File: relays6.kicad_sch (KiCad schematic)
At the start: 1 part

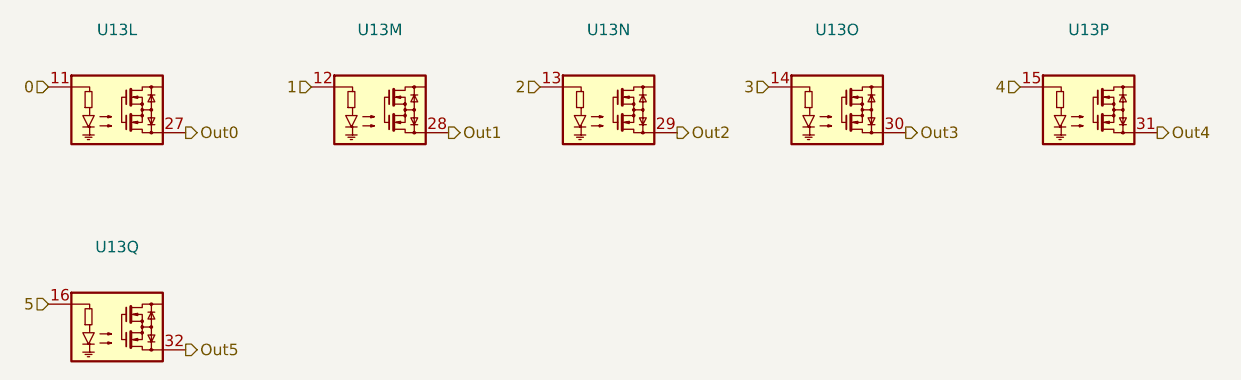
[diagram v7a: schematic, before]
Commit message: added footprints for modules
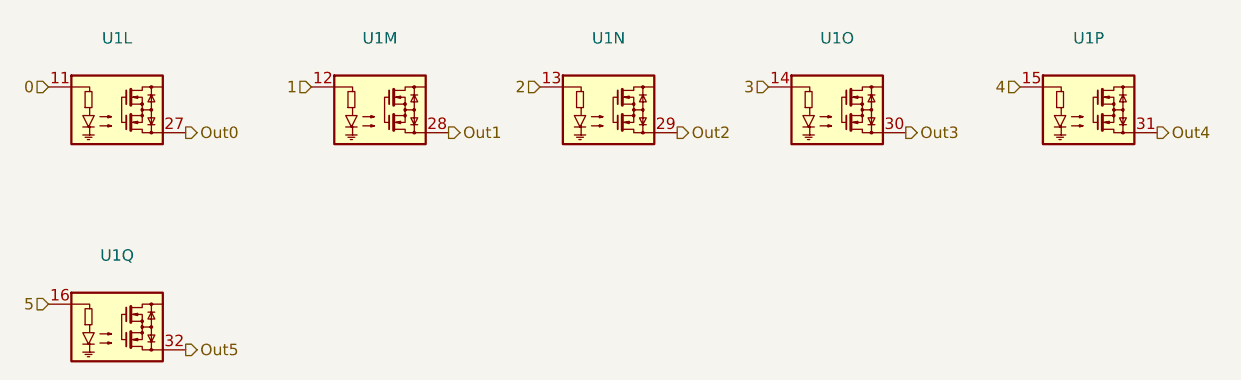
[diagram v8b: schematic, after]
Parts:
- U1: renamed from U13; footprint (none) -> custom:module_ssr
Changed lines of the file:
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@@
 		(dnp no)
 		(fields_autoplaced yes)
-		(property "Reference" "U13"
-			(at 180.34 83.82 0)
+		(property "Reference" "U1"
+			(at 180.34 84.7555 0)
 			(effects
 				(font
@@
 		)
 		(property "Value" "~"
-			(at 180.34 86.36 0)
-			(effects
-				(font
-					(size 1.27 1.27)
-				)
-			)
-		)
-		(property "Footprint" ""
+			(at 180.34 87.1798 0)
+			(effects
+				(font
+					(size 1.27 1.27)
+				)
+			)
+		)
+		(property "Footprint" "custom:module_ssr"
 			(at 176.53 87.63 0)
 			(effects
@@
 			(project "transistor-clock"
 				(path "/ce10d5bc-995e-4952-aa76-0a08f713a0f2/2c36a9e9-de42-4705-9ad4-94f4cc168e2f/a7714f05-6baa-4e42-8e1d-8ccd75369c94"
-					(reference "U13")
+					(reference "U1")
 					(unit 16)
 				)
 				(path "/ce10d5bc-995e-4952-aa76-0a08f713a0f2/2c36a9e9-de42-4705-9ad4-94f4cc168e2f/c8a6393e-4b34-48bb-b57a-38ecbb8960e5"
-					(reference "U23")
-					(unit 2)
+					(reference "U2")
+					(unit 16)
 				)
 			)
@@
 		(dnp no)
 		(fields_autoplaced yes)
-		(property "Reference" "U13"
-			(at 127 83.82 0)
+		(property "Reference" "U1"
+			(at 127 84.7555 0)
 			(effects
 				(font
@@
 		)
 		(property "Value" "~"
-			(at 127 86.36 0)
-			(effects
-				(font
-					(size 1.27 1.27)
-				)
-			)
-		)
-		(property "Footprint" ""
+			(at 127 87.1798 0)
+			(effects
+				(font
+					(size 1.27 1.27)
+				)
+			)
+		)
+		(property "Footprint" "custom:module_ssr"
 			(at 123.19 87.63 0)
 			(effects
@@
 			(project "transistor-clock"
 				(path "/ce10d5bc-995e-4952-aa76-0a08f713a0f2/2c36a9e9-de42-4705-9ad4-94f4cc168e2f/a7714f05-6baa-4e42-8e1d-8ccd75369c94"
-					(reference "U13")
+					(reference "U1")
 					(unit 14)
 				)
 				(path "/ce10d5bc-995e-4952-aa76-0a08f713a0f2/2c36a9e9-de42-4705-9ad4-94f4cc168e2f/c8a6393e-4b34-48bb-b57a-38ecbb8960e5"
-					(reference "U19")
-					(unit 2)
+					(reference "U2")
+					(unit 14)
 				)
 			)
@@
 		(dnp no)
 		(fields_autoplaced yes)
-		(property "Reference" "U13"
-			(at 72.39 107.95 0)
+		(property "Reference" "U1"
+			(at 72.39 108.8855 0)
 			(effects
 				(font
@@
 		)
 		(property "Value" "~"
-			(at 72.39 110.49 0)
-			(effects
-				(font
-					(size 1.27 1.27)
-				)
-			)
-		)
-		(property "Footprint" ""
+			(at 72.39 111.3098 0)
+			(effects
+				(font
+					(size 1.27 1.27)
+				)
+			)
+		)
+		(property "Footprint" "custom:module_ssr"
 			(at 68.58 111.76 0)
 			(effects
@@
 			(project "transistor-clock"
 				(path "/ce10d5bc-995e-4952-aa76-0a08f713a0f2/2c36a9e9-de42-4705-9ad4-94f4cc168e2f/a7714f05-6baa-4e42-8e1d-8ccd75369c94"
-					(reference "U13")
+					(reference "U1")
 					(unit 17)
 				)
 				(path "/ce10d5bc-995e-4952-aa76-0a08f713a0f2/2c36a9e9-de42-4705-9ad4-94f4cc168e2f/c8a6393e-4b34-48bb-b57a-38ecbb8960e5"
-					(reference "U25")
-					(unit 2)
+					(reference "U2")
+					(unit 17)
 				)
 			)
@@
 		(dnp no)
 		(fields_autoplaced yes)
-		(property "Reference" "U13"
-			(at 152.4 83.82 0)
+		(property "Reference" "U1"
+			(at 152.4 84.7555 0)
 			(effects
 				(font
@@
 		)
 		(property "Value" "~"
-			(at 152.4 86.36 0)
-			(effects
-				(font
-					(size 1.27 1.27)
-				)
-			)
-		)
-		(property "Footprint" ""
+			(at 152.4 87.1798 0)
+			(effects
+				(font
+					(size 1.27 1.27)
+				)
+			)
+		)
+		(property "Footprint" "custom:module_ssr"
 			(at 148.59 87.63 0)
 			(effects
@@
 			(project "transistor-clock"
 				(path "/ce10d5bc-995e-4952-aa76-0a08f713a0f2/2c36a9e9-de42-4705-9ad4-94f4cc168e2f/a7714f05-6baa-4e42-8e1d-8ccd75369c94"
-					(reference "U13")
+					(reference "U1")
 					(unit 15)
 				)
 				(path "/ce10d5bc-995e-4952-aa76-0a08f713a0f2/2c36a9e9-de42-4705-9ad4-94f4cc168e2f/c8a6393e-4b34-48bb-b57a-38ecbb8960e5"
-					(reference "U21")
-					(unit 2)
+					(reference "U2")
+					(unit 15)
 				)
 			)
@@
 		(dnp no)
 		(fields_autoplaced yes)
-		(property "Reference" "U13"
-			(at 72.39 83.82 0)
+		(property "Reference" "U1"
+			(at 72.39 84.7555 0)
 			(effects
 				(font
@@
 		)
 		(property "Value" "~"
-			(at 72.39 86.36 0)
-			(effects
-				(font
-					(size 1.27 1.27)
-				)
-			)
-		)
-		(property "Footprint" ""
+			(at 72.39 87.1798 0)
+			(effects
+				(font
+					(size 1.27 1.27)
+				)
+			)
+		)
+		(property "Footprint" "custom:module_ssr"
 			(at 68.58 87.63 0)
 			(effects
@@
 			(project "transistor-clock"
 				(path "/ce10d5bc-995e-4952-aa76-0a08f713a0f2/2c36a9e9-de42-4705-9ad4-94f4cc168e2f/a7714f05-6baa-4e42-8e1d-8ccd75369c94"
-					(reference "U13")
+					(reference "U1")
 					(unit 12)
 				)
 				(path "/ce10d5bc-995e-4952-aa76-0a08f713a0f2/2c36a9e9-de42-4705-9ad4-94f4cc168e2f/c8a6393e-4b34-48bb-b57a-38ecbb8960e5"
-					(reference "U15")
-					(unit 2)
+					(reference "U2")
+					(unit 12)
 				)
 			)
@@
 		(dnp no)
 		(fields_autoplaced yes)
-		(property "Reference" "U13"
-			(at 101.6 83.82 0)
+		(property "Reference" "U1"
+			(at 101.6 84.7555 0)
 			(effects
 				(font
@@
 		)
 		(property "Value" "~"
-			(at 101.6 86.36 0)
-			(effects
-				(font
-					(size 1.27 1.27)
-				)
-			)
-		)
-		(property "Footprint" ""
+			(at 101.6 87.1798 0)
+			(effects
+				(font
+					(size 1.27 1.27)
+				)
+			)
+		)
+		(property "Footprint" "custom:module_ssr"
 			(at 97.79 87.63 0)
 			(effects
@@
 			(project "transistor-clock"
 				(path "/ce10d5bc-995e-4952-aa76-0a08f713a0f2/2c36a9e9-de42-4705-9ad4-94f4cc168e2f/a7714f05-6baa-4e42-8e1d-8ccd75369c94"
-					(reference "U13")
+					(reference "U1")
 					(unit 13)
 				)
 				(path "/ce10d5bc-995e-4952-aa76-0a08f713a0f2/2c36a9e9-de42-4705-9ad4-94f4cc168e2f/c8a6393e-4b34-48bb-b57a-38ecbb8960e5"
-					(reference "U17")
-					(unit 2)
-				)
-			)
+					(reference "U2")
+					(unit 13)
+				)
+			)
